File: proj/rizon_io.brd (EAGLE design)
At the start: 87.6 x 72.9 mm, 32 parts, among them J1 DB9A-DS09AKG, P1 UART1(GND-TX-RX), P2 SCR0, P3 !IODEV[3..7], P4 VIN, P5 VCC_IO, U1 PC16550DPLCC, U10 74273PDIP, U11 74138PDIP, U2 7432PDIP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

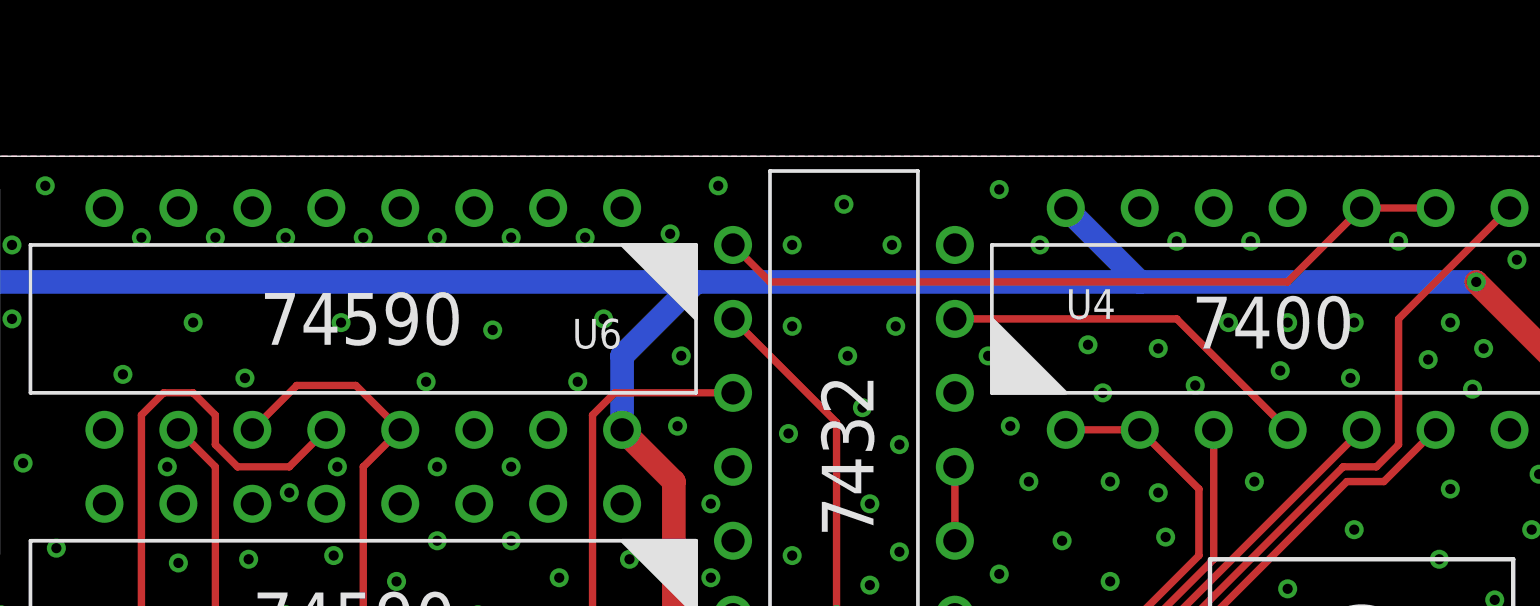
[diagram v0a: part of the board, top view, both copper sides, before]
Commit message: Added missing signal net (TIMER_OUT -> INT_TIMER) in Rizon I/O board Further routed SMD version of Rizon computer
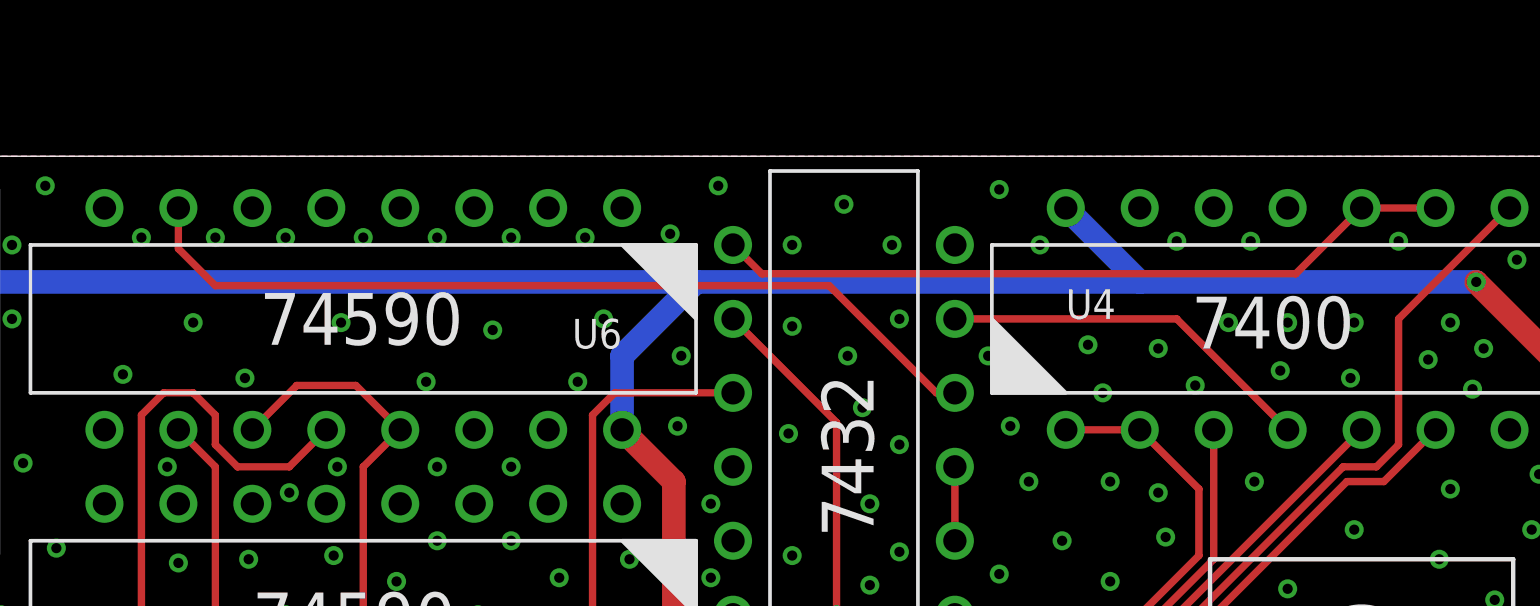
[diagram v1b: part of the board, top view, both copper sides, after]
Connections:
- removed net INT_TIMER: U2.P$5
- net TIMER_OUT: now also U2.P$5
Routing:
- net TIMER_OUT: track 0.00 -> 30.1 mm
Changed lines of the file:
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@@
 <via x="60.96" y="71.247" extent="1-16" drill="0.35"/>
 <via x="59.182" y="67.056" extent="1-16" drill="0.35"/>
-<via x="62.738" y="67.056" extent="1-16" drill="0.35"/>
+<via x="62.865" y="67.31" extent="1-16" drill="0.35"/>
 <via x="61.595" y="64.262" extent="1-16" drill="0.35"/>
 <via x="61.087" y="66.04" extent="1-16" drill="0.35"/>
@@
 <signal name="TIMER_OUT">
 <contactref element="U6" pad="P$7"/>
-</signal>
-<signal name="INT_TIMER">
 <contactref element="U2" pad="P$5"/>
+<wire x1="38.1" y1="71.12" x2="38.1" y2="69.723" width="0.254" layer="1"/>
+<wire x1="39.37" y1="68.453" x2="38.1" y2="69.723" width="0.254" layer="1"/>
+<wire x1="64.77" y1="64.77" x2="64.135" y2="64.77" width="0.254" layer="1"/>
+<wire x1="64.135" y1="64.77" x2="60.452" y2="68.453" width="0.254" layer="1"/>
+<wire x1="60.452" y1="68.453" x2="39.37" y2="68.453" width="0.254" layer="1"/>
 </signal>
 <signal name="INT_DEV">
@@
 <contactref element="U4" pad="P$9"/>
 <contactref element="U4" pad="P$10"/>
-<wire x1="57.15" y1="69.85" x2="58.42" y2="68.58" width="0.254" layer="1"/>
-<wire x1="76.2" y1="68.58" x2="78.74" y2="71.12" width="0.254" layer="1"/>
-<wire x1="58.42" y1="68.58" x2="76.2" y2="68.58" width="0.254" layer="1"/>
 <wire x1="78.74" y1="71.12" x2="81.28" y2="71.12" width="0.254" layer="1"/>
+<wire x1="57.15" y1="69.85" x2="58.1406" y2="68.8594" width="0.254" layer="1"/>
+<wire x1="76.4794" y1="68.8594" x2="78.74" y2="71.12" width="0.254" layer="1"/>
+<wire x1="58.1406" y1="68.8594" x2="76.4794" y2="68.8594" width="0.254" layer="1"/>
 </signal>
 <signal name="N$2">
